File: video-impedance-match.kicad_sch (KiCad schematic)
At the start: 11 parts

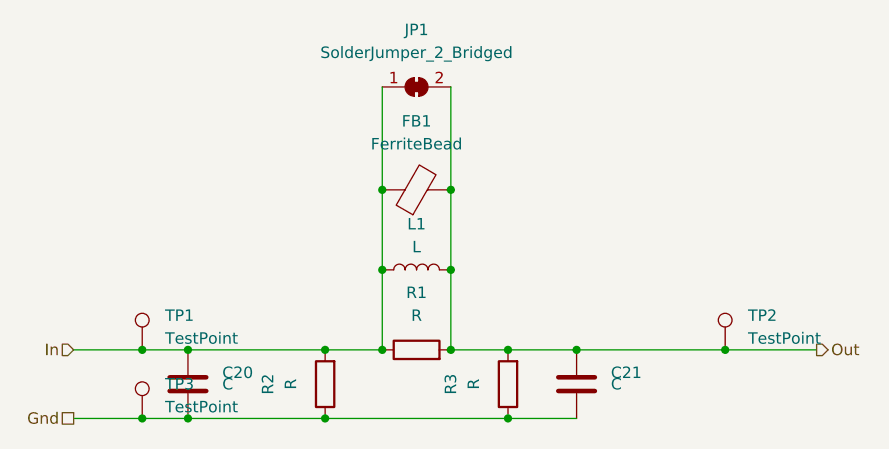
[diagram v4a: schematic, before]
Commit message: labels added
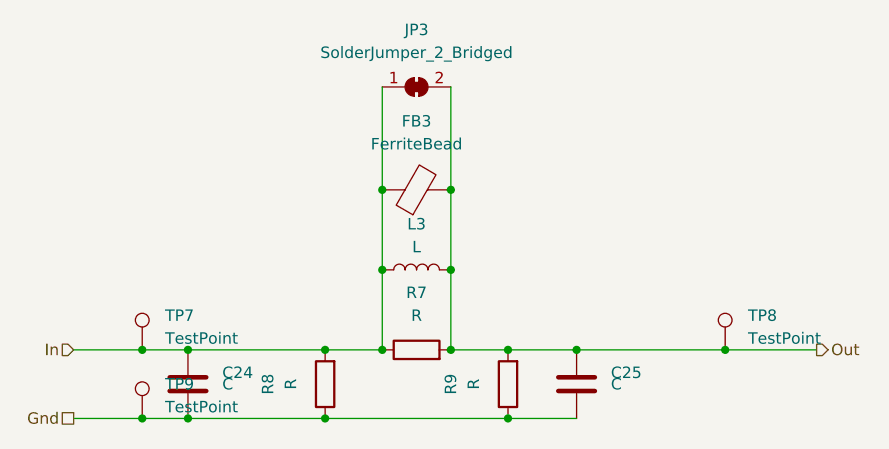
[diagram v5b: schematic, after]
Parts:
- renumbered C20 to C24, C21 to C25, FB1 to FB3, JP1 to JP3, L1 to L3, R1 to R7, R2 to R8, R3 to R9, TP1 to TP7, TP2 to TP8, TP3 to TP9
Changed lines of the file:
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@@
   (symbol (lib_id "Connector:TestPoint") (at 83.82 81.28 0)
     (in_bom yes) (on_board yes)
-    (property "Reference" "TP1" (id 0) (at 86.36 77.47 0)
+    (property "Reference" "TP7" (id 0) (at 86.36 77.47 0)
       (effects (font (size 1.27 1.27)) (justify left))
     )
@@
   (symbol (lib_id "Connector:TestPoint") (at 83.82 88.9 0)
     (in_bom yes) (on_board yes)
-    (property "Reference" "TP3" (id 0) (at 86.36 85.09 0)
+    (property "Reference" "TP9" (id 0) (at 86.36 85.09 0)
       (effects (font (size 1.27 1.27)) (justify left))
     )
@@
   (symbol (lib_id "Connector:TestPoint") (at 148.59 81.28 0)
     (in_bom yes) (on_board yes)
-    (property "Reference" "TP2" (id 0) (at 151.13 77.47 0)
+    (property "Reference" "TP8" (id 0) (at 151.13 77.47 0)
       (effects (font (size 1.27 1.27)) (justify left))
     )
@@
   (symbol (lib_id "Device:L") (at 114.3 72.39 90)
     (in_bom yes) (on_board yes)
-    (property "Reference" "L1" (id 0) (at 114.3 67.31 90))
+    (property "Reference" "L3" (id 0) (at 114.3 67.31 90))
     (property "Value" "L" (id 1) (at 114.3 69.85 90))
     (property "Footprint" "Resistor_SMD:R_1210_3225Metric" (id 2) (at 114.3 72.39 0)
@@
   (symbol (lib_id "Device:R") (at 104.14 85.09 180)
     (in_bom yes) (on_board yes)
-    (property "Reference" "R2" (id 0) (at 97.79 85.09 90))
+    (property "Reference" "R8" (id 0) (at 97.79 85.09 90))
     (property "Value" "R" (id 1) (at 100.33 85.09 90))
     (property "Footprint" "Resistor_SMD:R_0603_1608Metric" (id 2) (at 105.918 85.09 90)
@@
   (symbol (lib_id "Device:R") (at 114.3 81.28 90)
     (in_bom yes) (on_board yes)
-    (property "Reference" "R1" (id 0) (at 114.3 74.93 90))
+    (property "Reference" "R7" (id 0) (at 114.3 74.93 90))
     (property "Value" "R" (id 1) (at 114.3 77.47 90))
     (property "Footprint" "Resistor_SMD:R_0603_1608Metric" (id 2) (at 114.3 83.058 90)
@@
   (symbol (lib_id "Device:R") (at 124.46 85.09 180)
     (in_bom yes) (on_board yes)
-    (property "Reference" "R3" (id 0) (at 118.11 85.09 90))
+    (property "Reference" "R9" (id 0) (at 118.11 85.09 90))
     (property "Value" "R" (id 1) (at 120.65 85.09 90))
     (property "Footprint" "Resistor_SMD:R_0603_1608Metric" (id 2) (at 126.238 85.09 90)
@@
   (symbol (lib_id "Jumper:SolderJumper_2_Bridged") (at 114.3 52.07 0)
     (in_bom yes) (on_board yes)
-    (property "Reference" "JP1" (id 0) (at 114.3 45.72 0))
+    (property "Reference" "JP3" (id 0) (at 114.3 45.72 0))
     (property "Value" "SolderJumper_2_Bridged" (id 1) (at 114.3 48.26 0))
     (property "Footprint" "Jumper:SolderJumper-2_P1.3mm_Bridged_Pad1.0x1.5mm" (id 2) (at 114.3 52.07 0)
@@
   (symbol (lib_id "Device:C") (at 88.9 85.09 0)
     (in_bom yes) (on_board yes)
-    (property "Reference" "C20" (id 0) (at 92.71 83.82 0)
+    (property "Reference" "C24" (id 0) (at 92.71 83.82 0)
       (effects (font (size 1.27 1.27)) (justify left))
     )
@@
   (symbol (lib_id "Device:C") (at 132.08 85.09 0)
     (in_bom yes) (on_board yes)
-    (property "Reference" "C21" (id 0) (at 135.89 83.82 0)
+    (property "Reference" "C25" (id 0) (at 135.89 83.82 0)
       (effects (font (size 1.27 1.27)) (justify left))
     )
@@
   (symbol (lib_id "Device:FerriteBead") (at 114.3 63.5 90)
     (in_bom yes) (on_board yes)
-    (property "Reference" "FB1" (id 0) (at 114.3 55.88 90))
+    (property "Reference" "FB3" (id 0) (at 114.3 55.88 90))
     (property "Value" "FerriteBead" (id 1) (at 114.3 58.42 90))
     (property "Footprint" "Resistor_SMD:R_0603_1608Metric" (id 2) (at 114.3 65.278 90)

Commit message: Layout is basically complete, missing outline until dimensions can be double checked. DRC violations minimised but footprints (solder jumper and jamma edge connector) cause violations.
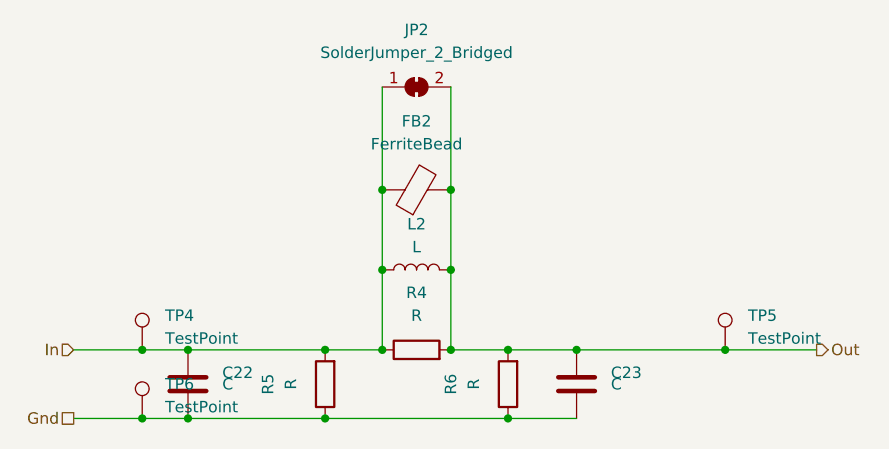
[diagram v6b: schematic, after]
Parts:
- JP2: renamed from JP3; footprint Jumper:SolderJumper-2_P1.3mm_Bridged_Pad1.0x1.5mm -> Jumper:SolderJumper-2_P1.3mm_Bridged_RoundedPad1.0x1.5mm
- renumbered C24 to C22, C25 to C23, FB3 to FB2, L3 to L2, R7 to R4, R8 to R5, R9 to R6, TP7 to TP4, TP8 to TP5, TP9 to TP6
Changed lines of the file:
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@@
 (kicad_sch (version 20201015) (generator eeschema)
-  (page 0 4)
   (paper "A4")
   (junction (at 83.82 81.28) (diameter 0.9144) (color 0 0 0 0))
@@
   (symbol (lib_id "Connector:TestPoint") (at 83.82 81.28 0)
     (in_bom yes) (on_board yes)
-    (property "Reference" "TP7" (id 0) (at 86.36 77.47 0)
+    (property "Reference" "TP4" (id 0) (at 86.36 77.47 0)
       (effects (font (size 1.27 1.27)) (justify left))
     )
@@
   (symbol (lib_id "Connector:TestPoint") (at 83.82 88.9 0)
     (in_bom yes) (on_board yes)
-    (property "Reference" "TP9" (id 0) (at 86.36 85.09 0)
+    (property "Reference" "TP6" (id 0) (at 86.36 85.09 0)
       (effects (font (size 1.27 1.27)) (justify left))
     )
@@
   (symbol (lib_id "Connector:TestPoint") (at 148.59 81.28 0)
     (in_bom yes) (on_board yes)
-    (property "Reference" "TP8" (id 0) (at 151.13 77.47 0)
+    (property "Reference" "TP5" (id 0) (at 151.13 77.47 0)
       (effects (font (size 1.27 1.27)) (justify left))
     )
@@
   (symbol (lib_id "Device:L") (at 114.3 72.39 90)
     (in_bom yes) (on_board yes)
-    (property "Reference" "L3" (id 0) (at 114.3 67.31 90))
+    (property "Reference" "L2" (id 0) (at 114.3 67.31 90))
     (property "Value" "L" (id 1) (at 114.3 69.85 90))
     (property "Footprint" "Resistor_SMD:R_1210_3225Metric" (id 2) (at 114.3 72.39 0)
@@
   (symbol (lib_id "Device:R") (at 104.14 85.09 180)
     (in_bom yes) (on_board yes)
-    (property "Reference" "R8" (id 0) (at 97.79 85.09 90))
+    (property "Reference" "R5" (id 0) (at 97.79 85.09 90))
     (property "Value" "R" (id 1) (at 100.33 85.09 90))
     (property "Footprint" "Resistor_SMD:R_0603_1608Metric" (id 2) (at 105.918 85.09 90)
@@
   (symbol (lib_id "Device:R") (at 114.3 81.28 90)
     (in_bom yes) (on_board yes)
-    (property "Reference" "R7" (id 0) (at 114.3 74.93 90))
+    (property "Reference" "R4" (id 0) (at 114.3 74.93 90))
     (property "Value" "R" (id 1) (at 114.3 77.47 90))
     (property "Footprint" "Resistor_SMD:R_0603_1608Metric" (id 2) (at 114.3 83.058 90)
@@
   (symbol (lib_id "Device:R") (at 124.46 85.09 180)
     (in_bom yes) (on_board yes)
-    (property "Reference" "R9" (id 0) (at 118.11 85.09 90))
+    (property "Reference" "R6" (id 0) (at 118.11 85.09 90))
     (property "Value" "R" (id 1) (at 120.65 85.09 90))
     (property "Footprint" "Resistor_SMD:R_0603_1608Metric" (id 2) (at 126.238 85.09 90)
@@
   (symbol (lib_id "Jumper:SolderJumper_2_Bridged") (at 114.3 52.07 0)
     (in_bom yes) (on_board yes)
-    (property "Reference" "JP3" (id 0) (at 114.3 45.72 0))
+    (property "Reference" "JP2" (id 0) (at 114.3 45.72 0))
     (property "Value" "SolderJumper_2_Bridged" (id 1) (at 114.3 48.26 0))
-    (property "Footprint" "Jumper:SolderJumper-2_P1.3mm_Bridged_Pad1.0x1.5mm" (id 2) (at 114.3 52.07 0)
+    (property "Footprint" "Jumper:SolderJumper-2_P1.3mm_Bridged_RoundedPad1.0x1.5mm" (id 2) (at 114.3 52.07 0)
       (effects (font (size 1.27 1.27)) hide)
     )
@@
   (symbol (lib_id "Device:C") (at 88.9 85.09 0)
     (in_bom yes) (on_board yes)
-    (property "Reference" "C24" (id 0) (at 92.71 83.82 0)
+    (property "Reference" "C22" (id 0) (at 92.71 83.82 0)
       (effects (font (size 1.27 1.27)) (justify left))
     )
@@
   (symbol (lib_id "Device:C") (at 132.08 85.09 0)
     (in_bom yes) (on_board yes)
-    (property "Reference" "C25" (id 0) (at 135.89 83.82 0)
+    (property "Reference" "C23" (id 0) (at 135.89 83.82 0)
       (effects (font (size 1.27 1.27)) (justify left))
     )
@@
   (symbol (lib_id "Device:FerriteBead") (at 114.3 63.5 90)
     (in_bom yes) (on_board yes)
-    (property "Reference" "FB3" (id 0) (at 114.3 55.88 90))
+    (property "Reference" "FB2" (id 0) (at 114.3 55.88 90))
     (property "Value" "FerriteBead" (id 1) (at 114.3 58.42 90))
     (property "Footprint" "Resistor_SMD:R_0603_1608Metric" (id 2) (at 114.3 65.278 90)
